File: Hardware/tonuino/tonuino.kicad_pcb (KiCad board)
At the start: 2 copper layers, 18 parts, among them J1 Conn_01x18_Female, J2 Conn_01x04_Female, J3 Conn_01x08_Female

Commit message: hardware: update pcbs
Signed-off-by: Tillmann Heidsieck <theidsieck@leenox.de>
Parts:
- removed D1, D2, D3: LED, LED_SMD:LED_0603_1608Metric
- removed J2: Conn_01x04_Female, Connector_PinHeader_2.54mm:PinHeader_2x02_P2.54mm_Vertical
- removed R7, R8: 150R, Resistor_SMD:R_0402_1005Metric
- removed the REF** at (166.4, 81.3)
- removed the REF** at (193.0, 132.1)
- added REF**: OSHW-Logo2_9.8x8mm_SilkScreen, Symbol:OSHW-Logo2_9.8x8mm_SilkScreen, F.Cu at (165.1, 81.3)
- R6: value 150R -> 0R
- moved R6 32.5 mm to (161.3, 104.1), turned to 90 degrees
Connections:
- A2 pad 3: Net-(A1-Pad5) -> Net-(A2-Pad3)
- R6 pad 1: Net-(D1-Pad1) -> Net-(A2-Pad3)
- R6 pad 2: Net-(J2-Pad1) -> Net-(A1-Pad5)
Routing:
- net Net-(D1-Pad1): track 57.1 -> 0.00 mm, vias 1 -> 0
- net Net-(D2-Pad1): track 38.2 -> 0.00 mm, vias 1 -> 0
- net Net-(D3-Pad1): track 17.8 -> 0.00 mm, vias 1 -> 0
- net Net-(J2-Pad1): track 13.5 -> 0.00 mm
- net Net-(J2-Pad3): track 12.8 -> 0.00 mm
- net Net-(J2-Pad2): track 10.1 -> 0.00 mm
- net Net-(D1-Pad2): track 4.69 -> 0.00 mm, vias 3 -> 0
- net Net-(A2-Pad3): track 0.00 -> 3.33 mm
- net Net-(A1-Pad5): track 18.7 -> 17.1 mm
- removed copper zone on B.Cu, net Net-(D1-Pad2)
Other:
- board outline added: 63.5 x 54.6 mm
- board text removed: "D3"

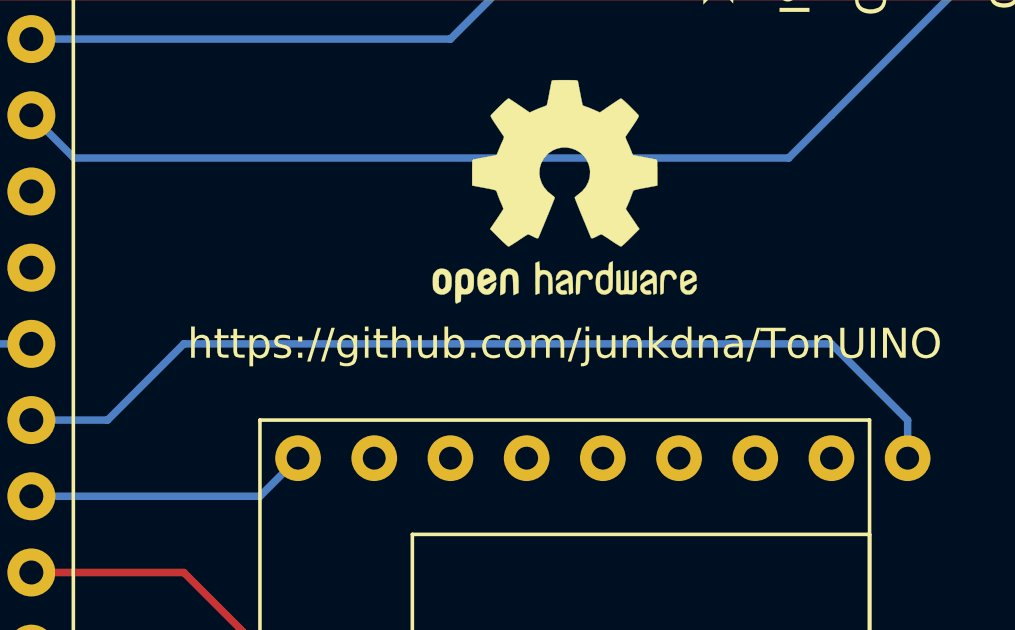
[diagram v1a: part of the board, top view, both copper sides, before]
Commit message: hardware: add additional pull-up for spk_en signal
Signed-off-by: Tillmann Heidsieck <theidsieck@leenox.de>
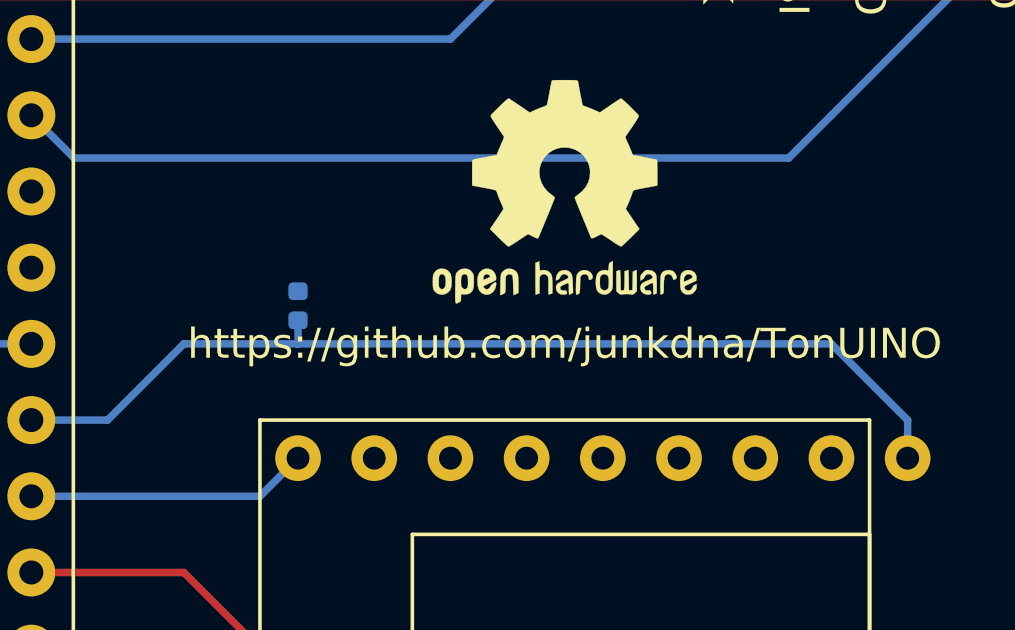
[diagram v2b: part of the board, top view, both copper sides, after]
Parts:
- added R7: 4k7, Resistor_SMD:R_0402_1005Metric, B.Cu at (156.2, 85.1)
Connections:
- net Net-(A1-Pad8) renamed /~SPK_EN
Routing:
- net /~SPK_EN: track 32.6 -> 33.4 mm

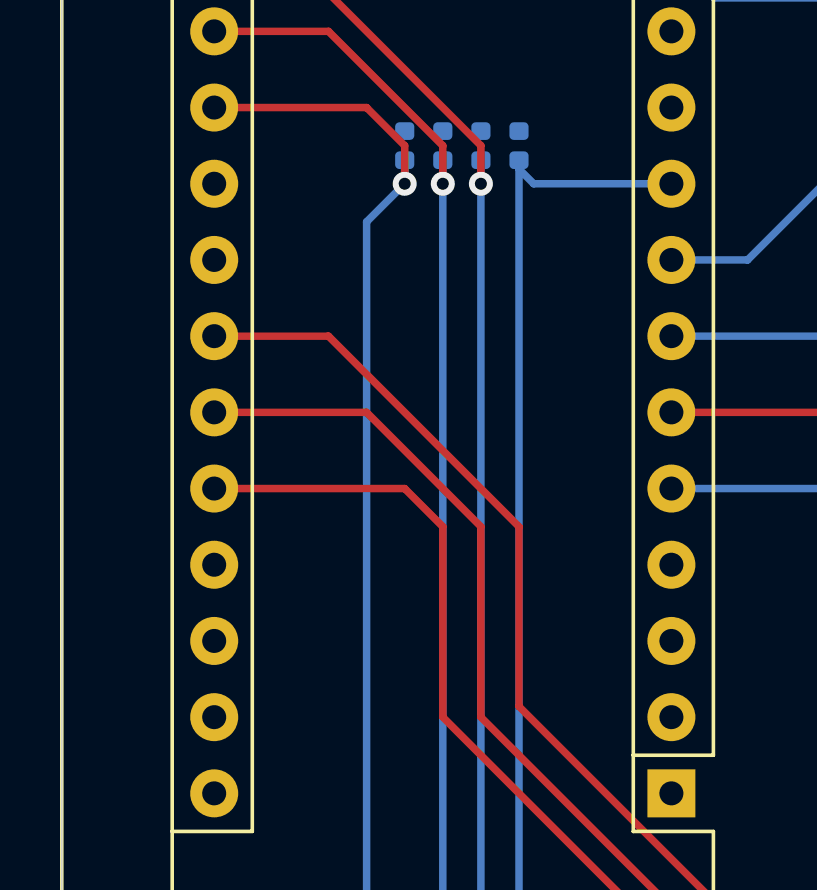
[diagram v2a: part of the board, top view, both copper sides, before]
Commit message: hardware: tonuino: fix LED pins, A6/7 are ADC only and wont work as outputs
Signed-off-by: Tillmann Heidsieck <theidsieck@leenox.de>
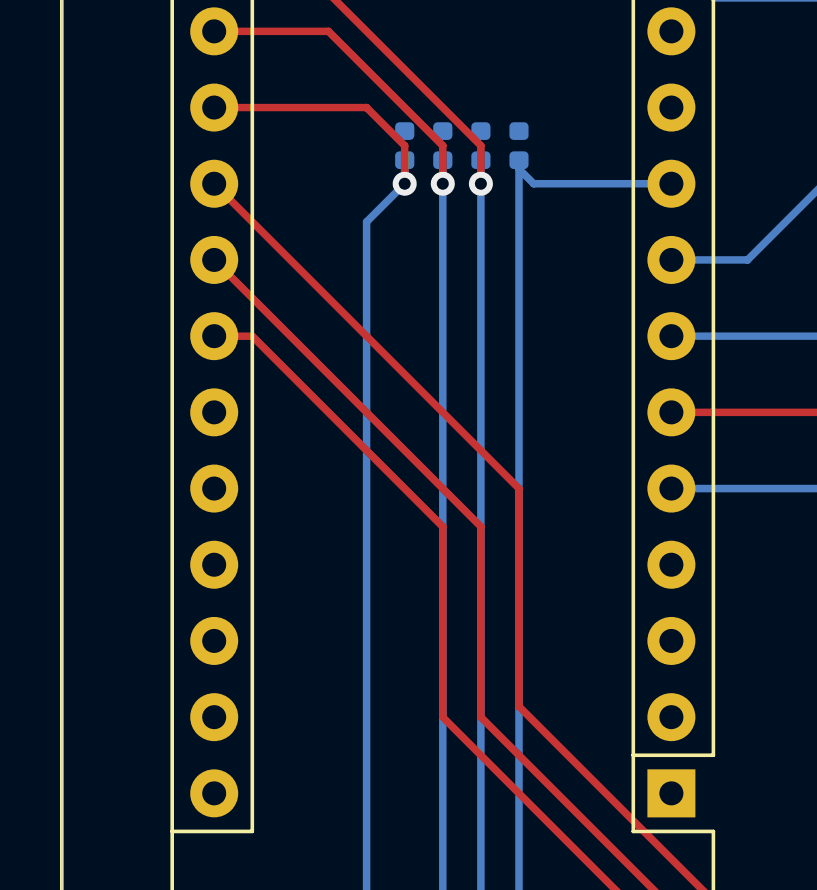
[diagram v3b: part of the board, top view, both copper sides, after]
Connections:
- A1 pad 22: Net-(A1-Pad22) -> /LED0
- A1 pad 23: Net-(A1-Pad23) -> /LED1
- A1 pad 24: /LED0 -> /LED2
- A1 pad 25: /LED1 -> Net-(A1-Pad25)
- A1 pad 26: /LED2 -> Net-(A1-Pad26)
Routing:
- net /LED0: track 42.7 -> 45.5 mm
- net /LED1: track 40.1 -> 42.2 mm
- net /LED2: track 36.5 -> 38.6 mm
